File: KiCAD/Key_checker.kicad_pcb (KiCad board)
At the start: 2 copper layers, 48.5 x 36 mm, 14 parts, among them Q1 Q_Photo_NPN, SW1 SW_DIP_x01, U1 ESP32-Dev-Module-ESP32-footpr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, U2 SSD1306

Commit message: Key Checker's PCB is Completed!
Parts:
- added G***: LOGO, other:Key_checker_logo, F.Cu at (174.0, 55.0)
- added J1: Conn_01x03_Male, Connector_PinHeader_2.54mm:PinHeader_1x03_P2.54mm_Horizontal, B.Cu at (199.0, 63.5)
- added J2: Conn_01x03_Male, Connector_PinHeader_2.54mm:PinHeader_1x03_P2.54mm_Horizontal, F.Cu at (159.7, 83.1)
- R6, R7: moved to F.Cu
- U1: value ESP32-Dev-Module-ESP32-footprints-Shem-Lib -> ESP32
- U2: footprint Connector_PinHeader_1.27mm:PinHeader_1x04_P1.27mm_Vertical -> Connector_PinHeader_2.54mm:PinHeader_1x04_P2.54mm_Vertical
- moved U2 89.2 mm to (207.6, 45.1), turned to 270 degrees
- moved R7 72.0 mm to (162.6, 48.3)
- moved RV1 68.5 mm to (193.0, 49.5)
- moved D1 67.6 mm to (158.1, 54.6), turned to 180 degrees
- moved D2 66.5 mm to (158.8, 63.5), turned to 180 degrees
- moved R6 66.3 mm to (162.6, 50.8)
- moved R3 65.6 mm to (179.1, 61.0), turned to 180 degrees
- moved R5 64.3 mm to (189.2, 50.8), turned to 90 degrees
- moved R1 62.8 mm to (156.8, 58.4)
- moved U1 62.3 mm to (172.7, 57.1)
- moved R2 57.4 mm to (179.1, 66.0), turned to 180 degrees
- moved R4 56.7 mm to (179.1, 63.5), turned to 180 degrees
- moved Q1 52.9 mm to (165.4, 80.5)
- moved SW1 40.1 mm to (190.8, 80.5)
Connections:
- net Net-(R5-Pad2) renamed +5V
- net Net-(R6-Pad1) renamed +3V3
- Q1 pad 1: Net-(Q1-Pad1) -> Net-(J2-Pad2)
- Q1 pad 2: GND -> Net-(J2-Pad1)
- R5 pad 1: Net-(R5-Pad1) -> Net-(J1-Pad3)
- RV1 pad 2: Net-(Q1-Pad1) -> Net-(J1-Pad2)
- SW1 pad 1: GND -> Net-(J2-Pad1)
- SW1 pad 2: Net-(R5-Pad1) -> Net-(J2-Pad3)
- U1 pad 13: Net-(Q1-Pad1) -> Net-(J1-Pad2)
- U1 pad 6: Net-(R5-Pad1) -> Net-(J1-Pad3)
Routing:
- net Net-(J1-Pad3): track 0.00 -> 58.3 mm
- net Net-(Q1-Pad1): track 44.7 -> 0.00 mm
- net Net-(J1-Pad2): track 0.00 -> 40.3 mm
- net +3V3: track 44.7 -> 80.0 mm
- net Net-(R4-Pad1): track 43.4 -> 8.60 mm
- net Net-(J2-Pad3): track 0.00 -> 32.5 mm
- net Net-(J2-Pad1): track 0.00 -> 28.0 mm
- net Net-(R5-Pad1): track 25.9 -> 0.00 mm
- net Net-(R6-Pad2): track 30.1 -> 52.4 mm
- net Net-(D2-Pad4): track 8.70 -> 29.1 mm
- net Net-(D2-Pad1): track 2.90 -> 20.5 mm
- net Net-(D2-Pad2): track 6.16 -> 22.4 mm
- net Net-(R7-Pad2): track 30.6 -> 46.5 mm
- net +5V: track 23.2 -> 10.1 mm
- net Net-(R2-Pad1): track 13.1 -> 3.96 mm
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- added copper zone on F.Cu, net (none)
- added copper zone on B.Cu, net Net-(J2-Pad1)
- added copper zone on F.Cu, net Net-(J2-Pad1)
- removed copper zone on F.Cu, net GND
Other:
- board size 48.5 x 36 mm -> 64.8 x 45 mm

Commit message: fixed PCB
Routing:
- added copper zone on B.Cu, net Net-(J2-Pad2)
- added copper zone on F.Cu, net Net-(J2-Pad2)
- removed copper zone on B.Cu, net Net-(J2-Pad1)
- removed copper zone on F.Cu, net Net-(J2-Pad1)
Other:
- outline, holes or cut-outs redrawn
- board text added: "Key Checker Rev1.0 by Chrodream"
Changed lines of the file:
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@@
   (general
     (thickness 1.6)
-    (drawings 15)
+    (drawings 30)
     (tracks 82)
     (zones 0)
@@
     )
   )
+  (gr_text "Key Checker Rev1.0\nby Chrodream" (at 208.28 64.135 90) (layer B.SilkS)
+    (effects (font (size 1 1) (thickness 0.15)) (justify mirror))
+  )
+  (gr_line (start 208.915 73.66) (end 200.66 73.66) (layer Edge.Cuts) (width 0.05))
+  (gr_line (start 200.66 74.93) (end 211.09 74.93) (layer Edge.Cuts) (width 0.05))
+  (gr_line (start 195.58 74.93) (end 168.275 74.93) (layer Edge.Cuts) (width 0.05))
+  (gr_line (start 168.275 73.66) (end 195.58 73.66) (layer Edge.Cuts) (width 0.05))
+  (gr_line (start 163.195 74.93) (end 147.59 74.93) (layer Edge.Cuts) (width 0.05))
+  (gr_line (start 163.195 73.66) (end 149.225 73.66) (layer Edge.Cuts) (width 0.05))
+  (gr_arc (start 200.66 74.295) (end 200.66 73.66) (angle -180) (layer Edge.Cuts) (width 0.05))
+  (gr_arc (start 195.58 74.295) (end 195.58 74.93) (angle -180) (layer Edge.Cuts) (width 0.05))
+  (gr_arc (start 168.275 74.295) (end 168.275 73.66) (angle -180) (layer Edge.Cuts) (width 0.05))
+  (gr_arc (start 163.195 74.295) (end 163.195 74.93) (angle -180) (layer Edge.Cuts) (width 0.05))
+  (gr_circle (center 199.39 74.295) (end 199.39 73.66) (layer Edge.Cuts) (width 0.05))
+  (gr_circle (center 198.12 74.295) (end 198.12 74.93) (layer Edge.Cuts) (width 0.05))
+  (gr_circle (center 196.85 74.295) (end 196.85 74.93) (layer Edge.Cuts) (width 0.05))
+  (gr_circle (center 167.005 74.295) (end 167.005 74.93) (layer Edge.Cuts) (width 0.05))
+  (gr_circle (center 164.465 74.295) (end 164.465 74.93) (layer Edge.Cuts) (width 0.05))
+  (gr_circle (center 165.735 74.295) (end 165.735 74.93) (layer Edge.Cuts) (width 0.05))
   (gr_circle (center 206 81) (end 206 84) (layer Edge.Cuts) (width 0.05))
   (gr_circle (center 174 81) (end 174 84) (layer Edge.Cuts) (width 0.05))
-  (gr_line (start 147.59 85.63) (end 147.59 75.47) (layer Edge.Cuts) (width 0.05))
+  (gr_line (start 147.59 85.63) (end 147.59 74.93) (layer Edge.Cuts) (width 0.05))
   (gr_line (start 211.09 85.63) (end 147.59 85.63) (layer Edge.Cuts) (width 0.05))
-  (gr_line (start 211.09 75.47) (end 211.09 85.63) (layer Edge.Cuts) (width 0.05))
-  (gr_line (start 147.59 75.47) (end 211.09 75.47) (layer Edge.Cuts) (width 0.05))
+  (gr_line (start 211.09 74.93) (end 211.09 85.63) (layer Edge.Cuts) (width 0.05))
   (gr_circle (center 206 51.5) (end 206 54.5) (layer Edge.Cuts) (width 0.05))
-  (gr_line (start 208.915 73.66) (end 149.225 73.66) (layer Edge.Cuts) (width 0.05))
   (gr_line (start 149.225 40.64) (end 208.915 40.64) (layer Edge.Cuts) (width 0.05))
   (gr_arc (start 208.915 71.12) (end 208.915 73.66) (angle -90) (layer Edge.Cuts) (width 0.05))
@@
     )
   )
-  (zone (net 42) (net_name "Net-(J2-Pad1)") (layer B.Cu) (hatch edge 0.508)
+  (zone (net 41) (net_name "Net-(J2-Pad2)") (layer F.Cu) (hatch edge 0.508)
     (connect_pads (clearance 0.508))
     (min_thickness 0.254)
@@
     (polygon
       (pts
-        (xy 211.5 86) (xy 147.5 86) (xy 147.5 75) (xy 211.5 75)
+        (xy 211.455 85.725) (xy 147.32 85.725) (xy 147.32 74.93) (xy 211.455 74.93)
       )
     )
   )
-  (zone (net 42) (net_name "Net-(J2-Pad1)") (layer F.Cu) (hatch edge 0.508)
+  (zone (net 41) (net_name "Net-(J2-Pad2)") (layer B.Cu) (hatch edge 0.508)
     (connect_pads (clearance 0.508))
     (min_thickness 0.254)
@@
     (polygon
       (pts
-        (xy 211.5 86) (xy 147.5 86) (xy 147.5 75) (xy 211.5 75)
+        (xy 211.455 85.725) (xy 147.32 85.725) (xy 147.32 74.93) (xy 211.455 74.93)
       )
     )

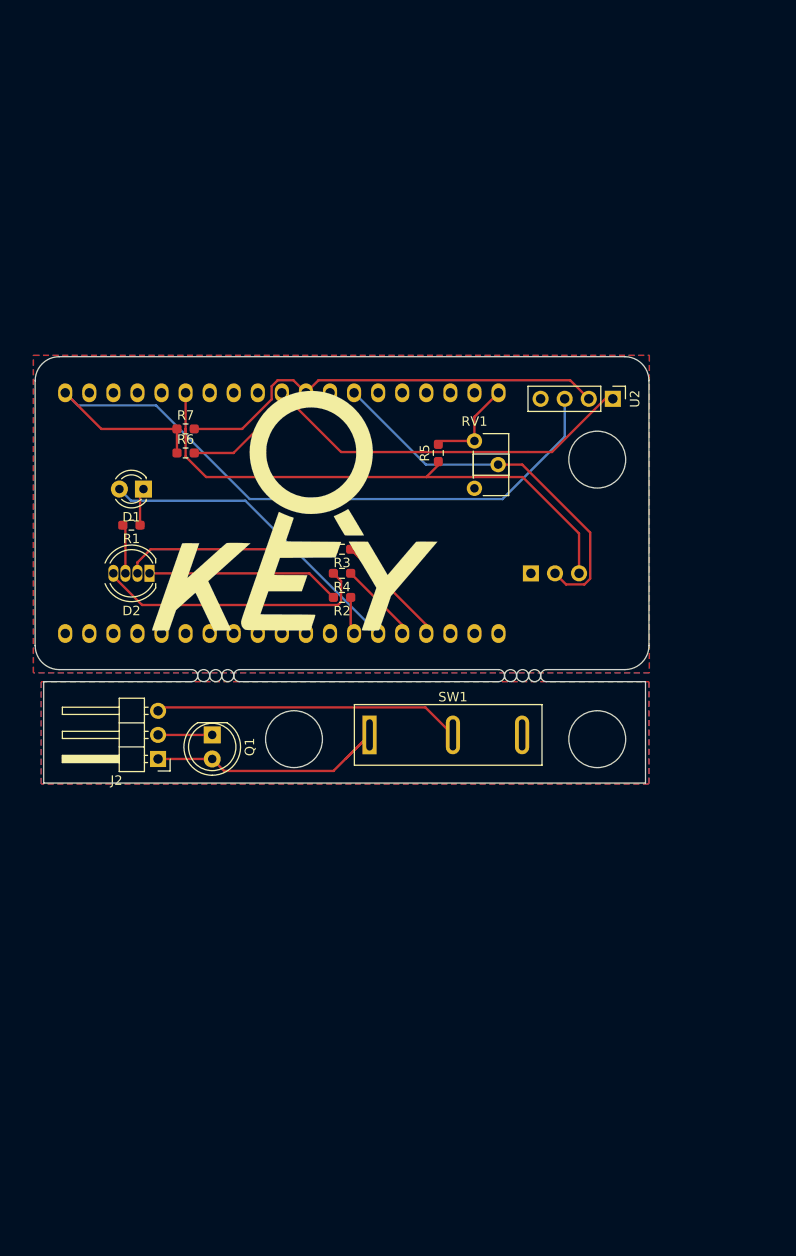
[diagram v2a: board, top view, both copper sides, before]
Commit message: PCB is changed
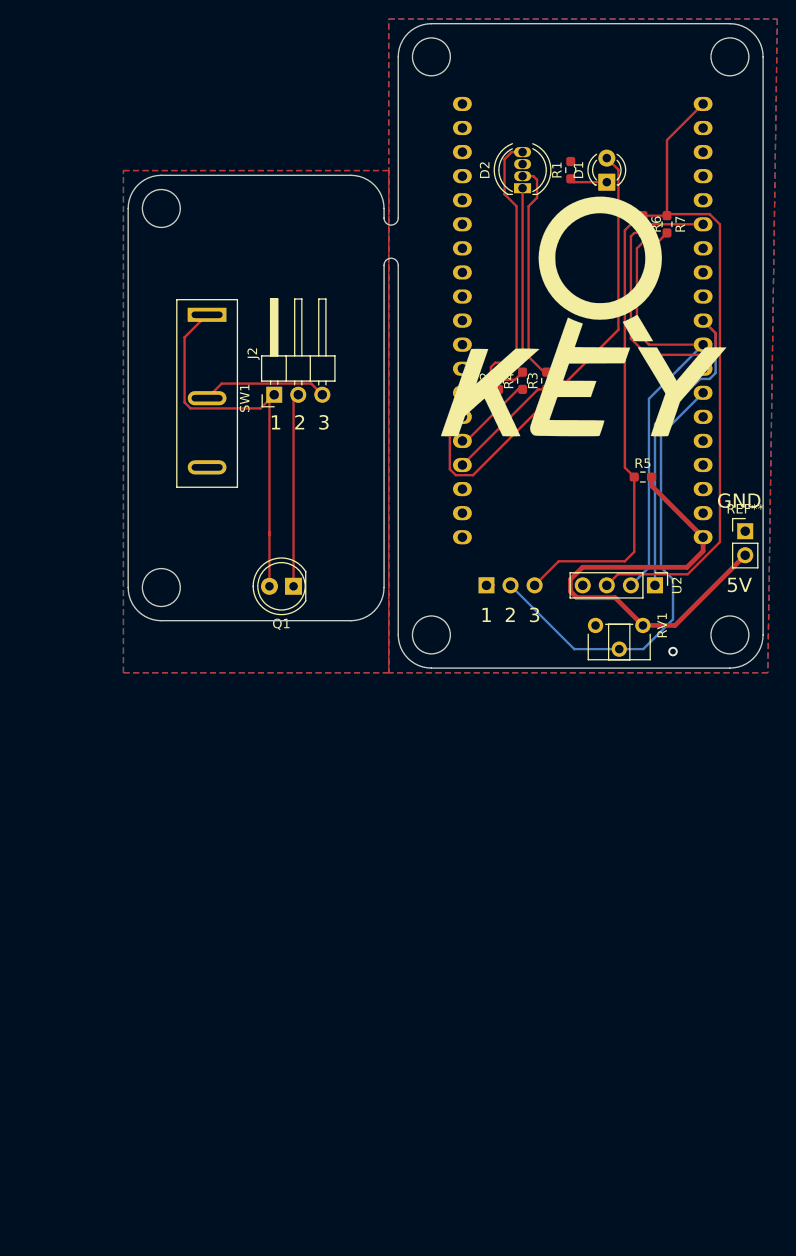
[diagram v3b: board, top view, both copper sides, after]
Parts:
- added REF**: PinHeader_1x02_P2.54mm_Vertical, Connector_PinHeader_2.54mm:PinHeader_1x02_P2.54mm_Vertical, F.Cu at (221.6, 59.1)
- moved R1 59.6 mm to (203.2, 21.0), turned to 90 degrees
- moved D1 58.6 mm to (207.0, 22.2), turned to 90 degrees
- moved D2 56.6 mm to (198.1, 22.9), turned to 90 degrees
- moved R7 55.2 mm to (213.4, 26.7), turned to 270 degrees
- moved R6 54.0 mm to (210.8, 26.7), turned to 270 degrees
- moved SW1 44.0 mm to (164.8, 45.0), turned to 270 degrees
- moved J2 40.3 mm to (171.9, 44.7), turned to 90 degrees
- moved U1 37.7 mm to (204.5, 36.8), turned to 270 degrees
- moved G*** 36.7 mm to (204.5, 34.5)
- moved R2 28.2 mm to (195.6, 43.2), turned to 90 degrees
- moved R3 28.0 mm to (200.7, 43.2), turned to 90 degrees
- moved R4 27.9 mm to (198.1, 43.2), turned to 90 degrees
- moved RV1 26.4 mm to (210.8, 69.0), turned to 270 degrees
- moved R5 21.7 mm to (210.8, 53.3), turned to 0 degrees
- moved U2 20.2 mm to (212.1, 64.8)
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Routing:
- net +5V: track 10.1 -> 49.6 mm
- net Net-(J2-Pad3): track 32.5 -> 13.3 mm
- net Net-(D1-Pad2): track 33.6 -> 49.1 mm
- net Net-(J2-Pad2): track 5.72 -> 20.4 mm
- net Net-(J2-Pad1): track 28.0 -> 41.2 mm
- net +3V3: track 80.0 -> 69.4 mm
- net Net-(J1-Pad2): track 40.3 -> 47.5 mm
- net Net-(R6-Pad2): track 52.4 -> 57.4 mm
- net GND: track 5.19 -> 0.80 mm, vias 0 -> 1
- net Net-(J1-Pad3): track 58.3 -> 54.8 mm
- net Net-(D2-Pad4): track 29.1 -> 31.6 mm
- net Net-(R7-Pad2): track 46.5 -> 48.8 mm
- net Net-(D2-Pad2): track 22.4 -> 23.3 mm
- net Net-(D2-Pad1): track 20.5 -> 21.0 mm
- added copper zone on F.Cu, net GND
- added copper zone on B.Cu, net Net-(J2-Pad1)
- added copper zone on F.Cu, net Net-(J2-Pad1)
- removed copper zone on F.Cu, net (none)
- removed copper zone on B.Cu, net Net-(J2-Pad2)
- removed copper zone on F.Cu, net Net-(J2-Pad2)
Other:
- board size 64.8 x 45 mm -> 67 x 68 mm
- board text added: "1"
- board text added: "2"
- board text added: "3"
- board text added: "5V"
- board text added: "GND"
- board text removed: "Key Checker Rev1.0 by Chrodream"
